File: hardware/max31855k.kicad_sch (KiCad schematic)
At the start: 6 parts, among them U2 MAX31855KASA

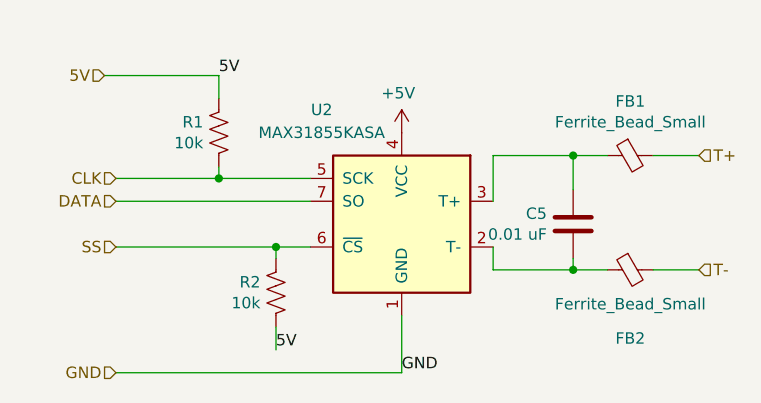
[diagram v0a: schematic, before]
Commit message: added historical scripts and new revisions
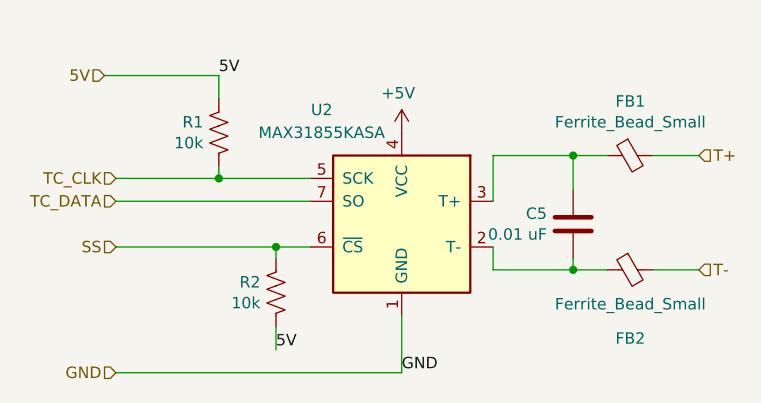
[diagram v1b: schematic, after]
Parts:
- U2: TC_DATAsheet (none) -> http://TC_DATAsheets.maximintegrated.com/en/ds/MAX31855.pdf
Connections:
- net CLK renamed TC_CLK
- net DATA renamed TC_DATA
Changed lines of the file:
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@@
 		)
 	)
-	(hierarchical_label "CLK"
+	(hierarchical_label "TC_CLK"
 		(shape input)
 		(at 113.03 66.04 180)
@@
 		)
 	)
-	(hierarchical_label "DATA"
+	(hierarchical_label "TC_DATA"
 		(shape input)
 		(at 113.03 68.58 180)
@@
 			)
 		)
-		(property "Datasheet" "http://datasheets.maximintegrated.com/en/ds/MAX31855.pdf"
+		(property "TC_DATAsheet" "http://TC_DATAsheets.maximintegrated.com/en/ds/MAX31855.pdf"
 			(at 144.78 71.12 0)
 			(effects
@@
 			)
 		)
-		(property "Datasheet" ""
+		(property "TC_DATAsheet" ""
 			(at 144.78 60.96 0)
 			(effects
@@
 			)
 		)
-		(property "Datasheet" "~"
+		(property "TC_DATAsheet" "~"
 			(at 170.18 63.5 0)
 			(effects
@@
 			)
 		)
-		(property "Datasheet" "~"
+		(property "TC_DATAsheet" "~"
 			(at 130.81 78.74 0)
 			(effects
@@
 			)
 		)
-		(property "Datasheet" "~"
+		(property "TC_DATAsheet" "~"
 			(at 163.83 71.12 0)
 			(effects
@@
 			)
 		)
-		(property "Datasheet" "~"
+		(property "TC_DATAsheet" "~"
 			(at 124.46 60.96 0)
 			(effects
@@
 			)
 		)
-		(property "Datasheet" "~"
+		(property "TC_DATAsheet" "~"
 			(at 170.18 76.2 0)
 			(effects

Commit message: review and revise for current template and kmlib; still needs updating
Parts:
- removed R1, R2: 10k, Resistor_SMD:R_1206_3216Metric_Pad1.30x1.75mm_HandSolder, symbol Device:R_US
- added R1, R2: 10k, Resistor_SMD:R_1206_3216Metric_Pad1.30x1.75mm_HandSolder, symbol Device:R
- C5: value 0.01 uF -> 10n
- FB1, FB2: symbol BREAD_Slice-rescue:Ferrite_Bead_Small-Device -> Device:FerriteBead_Small
- U2: symbol BREAD_Slice-rescue:MAX31855KASA-Sensor_Temperature -> Sensor_Temperature:MAX31855KASA
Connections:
- net 5V: now also R1.1, R2.2
- net SS: now also R2.1
- net TC_CLK: now also R1.2
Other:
- moved on the sheet: U2
